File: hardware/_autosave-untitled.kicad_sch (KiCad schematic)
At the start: 39 parts, among them J5 USB4105-GF-A, J6 DCJ200-10-A-K1-K, SW1 SW_Push, SW2 SW_Push, SW3 RA1113112R, U3 USBLC6-2SC6, U4 NCP1117ST33T3G, U5 ESP32-S3-WROOM-1-N8R8

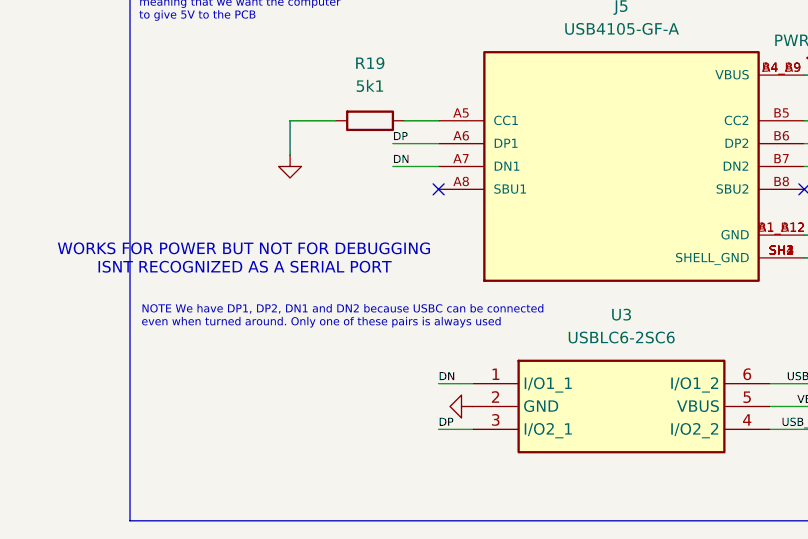
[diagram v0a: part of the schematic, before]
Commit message: Tried to prevent crosstalk, fixed silkscreen, changes to fit DFM
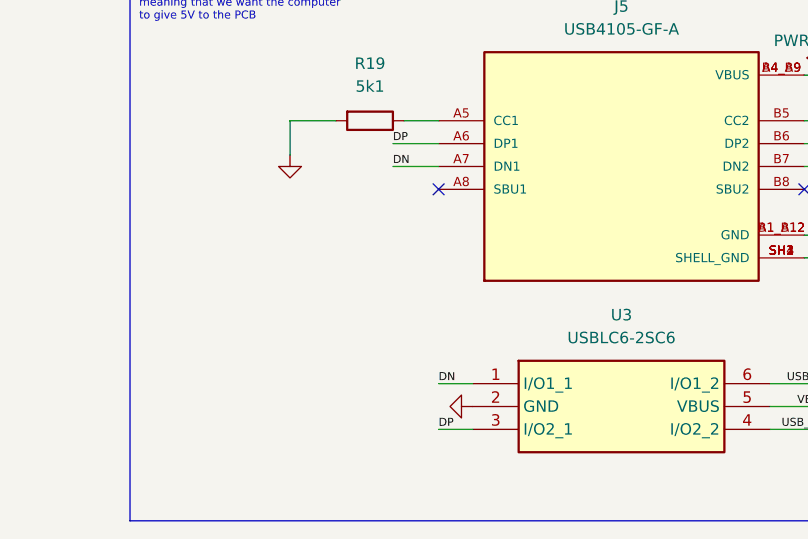
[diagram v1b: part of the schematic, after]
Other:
- note removed: "NOTE We have DP1, DP2, DN1 and DN2 because USBC can be connected even when turned around. Only one of these pairs is always used"
- note removed: "WORKS FOR POWER BUT NOT FOR DEBUGGING ISNT RECOGNIZED AS A SERIAL PORT"
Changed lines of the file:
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@@
-		)
-	)
-	(text "WORKS FOR POWER BUT NOT FOR DEBUGGING\nISNT RECOGNIZED AS A SERIAL PORT"
-		(exclude_from_sim no)
-		(at 35.56 166.624 0)
-		(effects
-			(font
-				(size 1.27 1.27)
-				(color 19 255 0 1)
-			)
 		)
 	)
@@
 		)
 	)
-	(text "NOTE We have DP1, DP2, DN1 and DN2 because USBC can be connected\neven when turned around. Only one of these pairs is always used"
-		(exclude_from_sim no)
-		(at 24.13 172.974 0)
-		(effects
-			(font
-				(size 0.889 0.889)
-				(color 255 0 7 1)
-			)
-			(justify left)
-		)
-	)
